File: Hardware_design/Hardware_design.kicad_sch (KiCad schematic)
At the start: 46 parts, among them IC1 ESP32-S3-WROOM-1-N16, J1 FTSH-103-01-F-D, J2 SBH11-PBPC-D05-ST-BK, J3 54-00131, SW1 TL3301FF160QG, SW2 TL3301FF160QG, U1 LS7366R-S, U2 TXB0104DR, U3 LP3875EMP-3.3

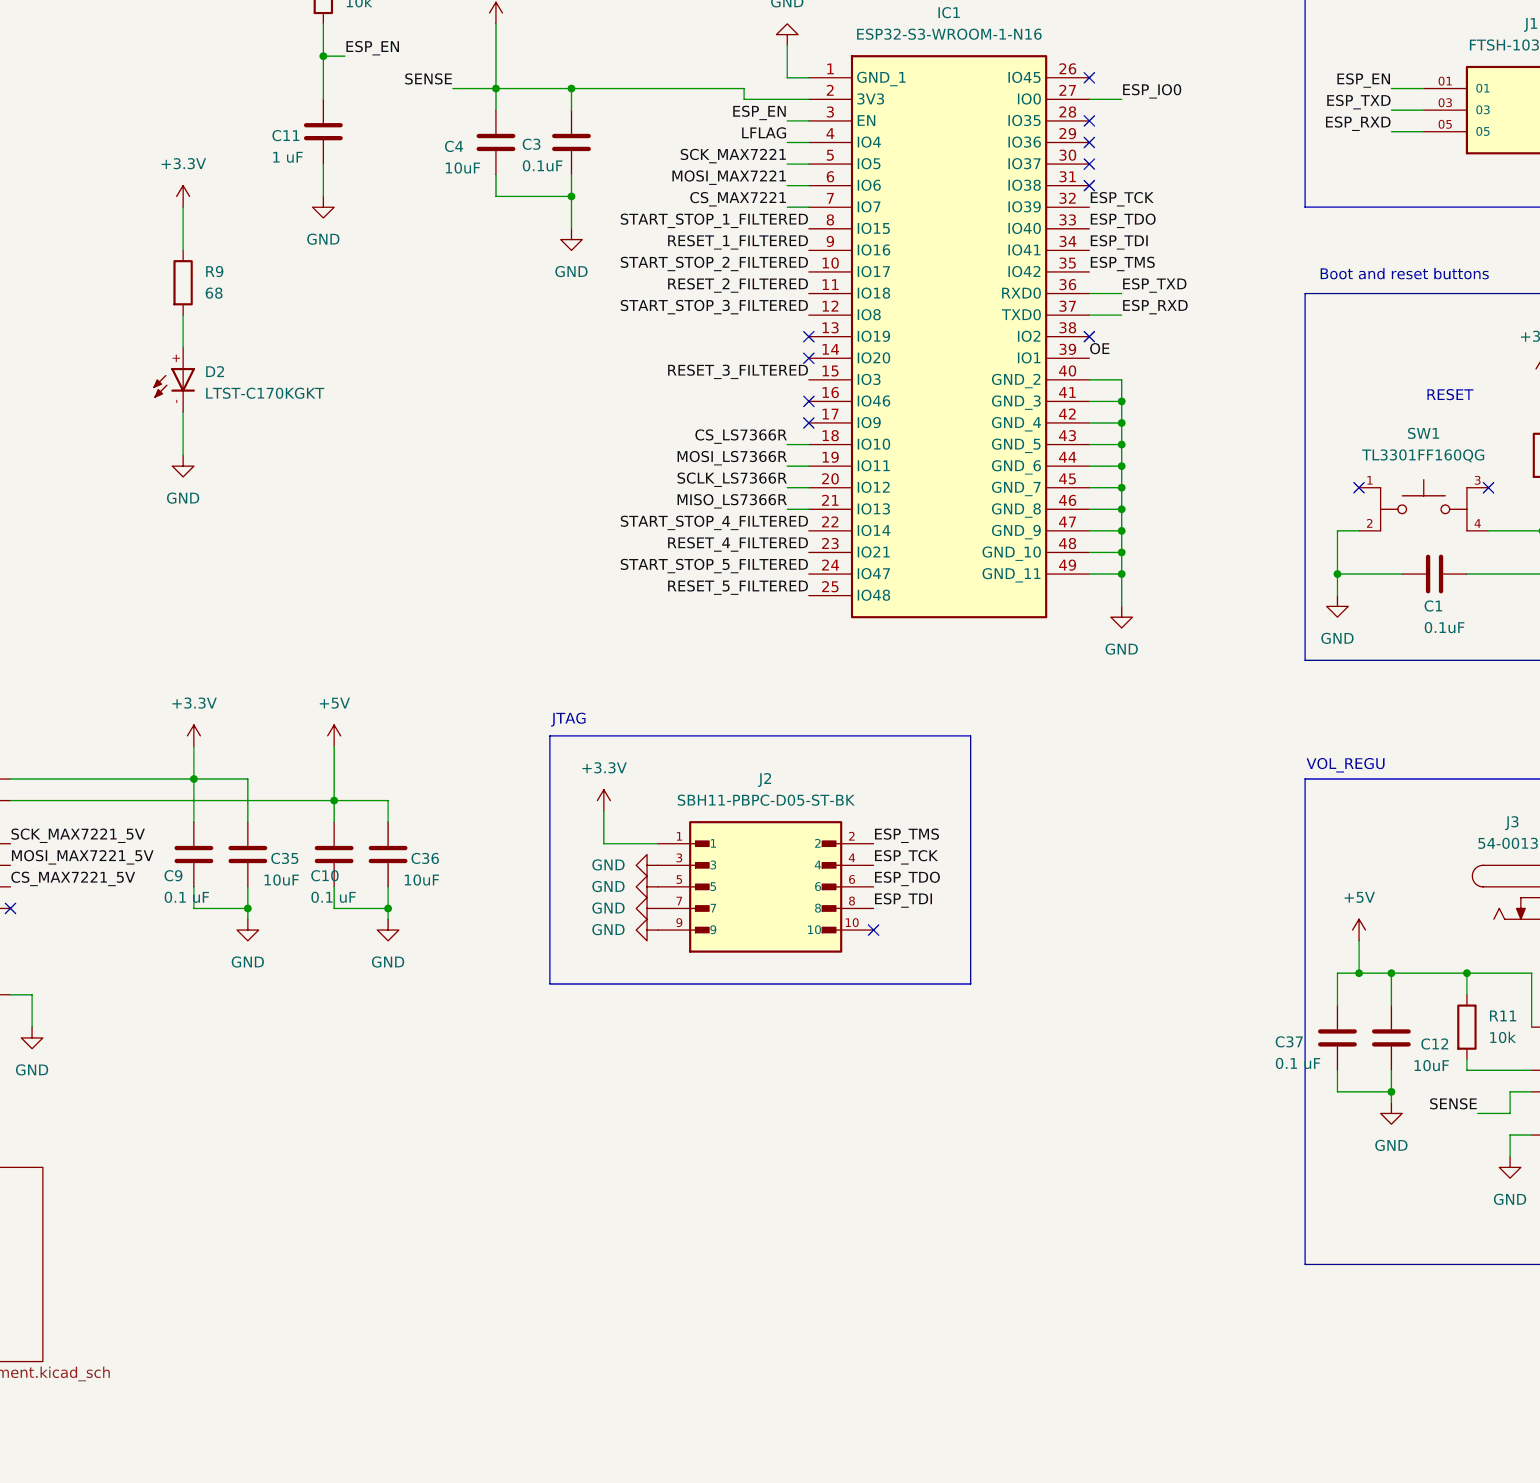
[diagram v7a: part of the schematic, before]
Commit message: component placement started
index pin and gpio pins for 10 buttons problem, index pin should be activated whenever any of the 10 buttons is pressed but only the gpio pin of the button that was pressed should also be activaded
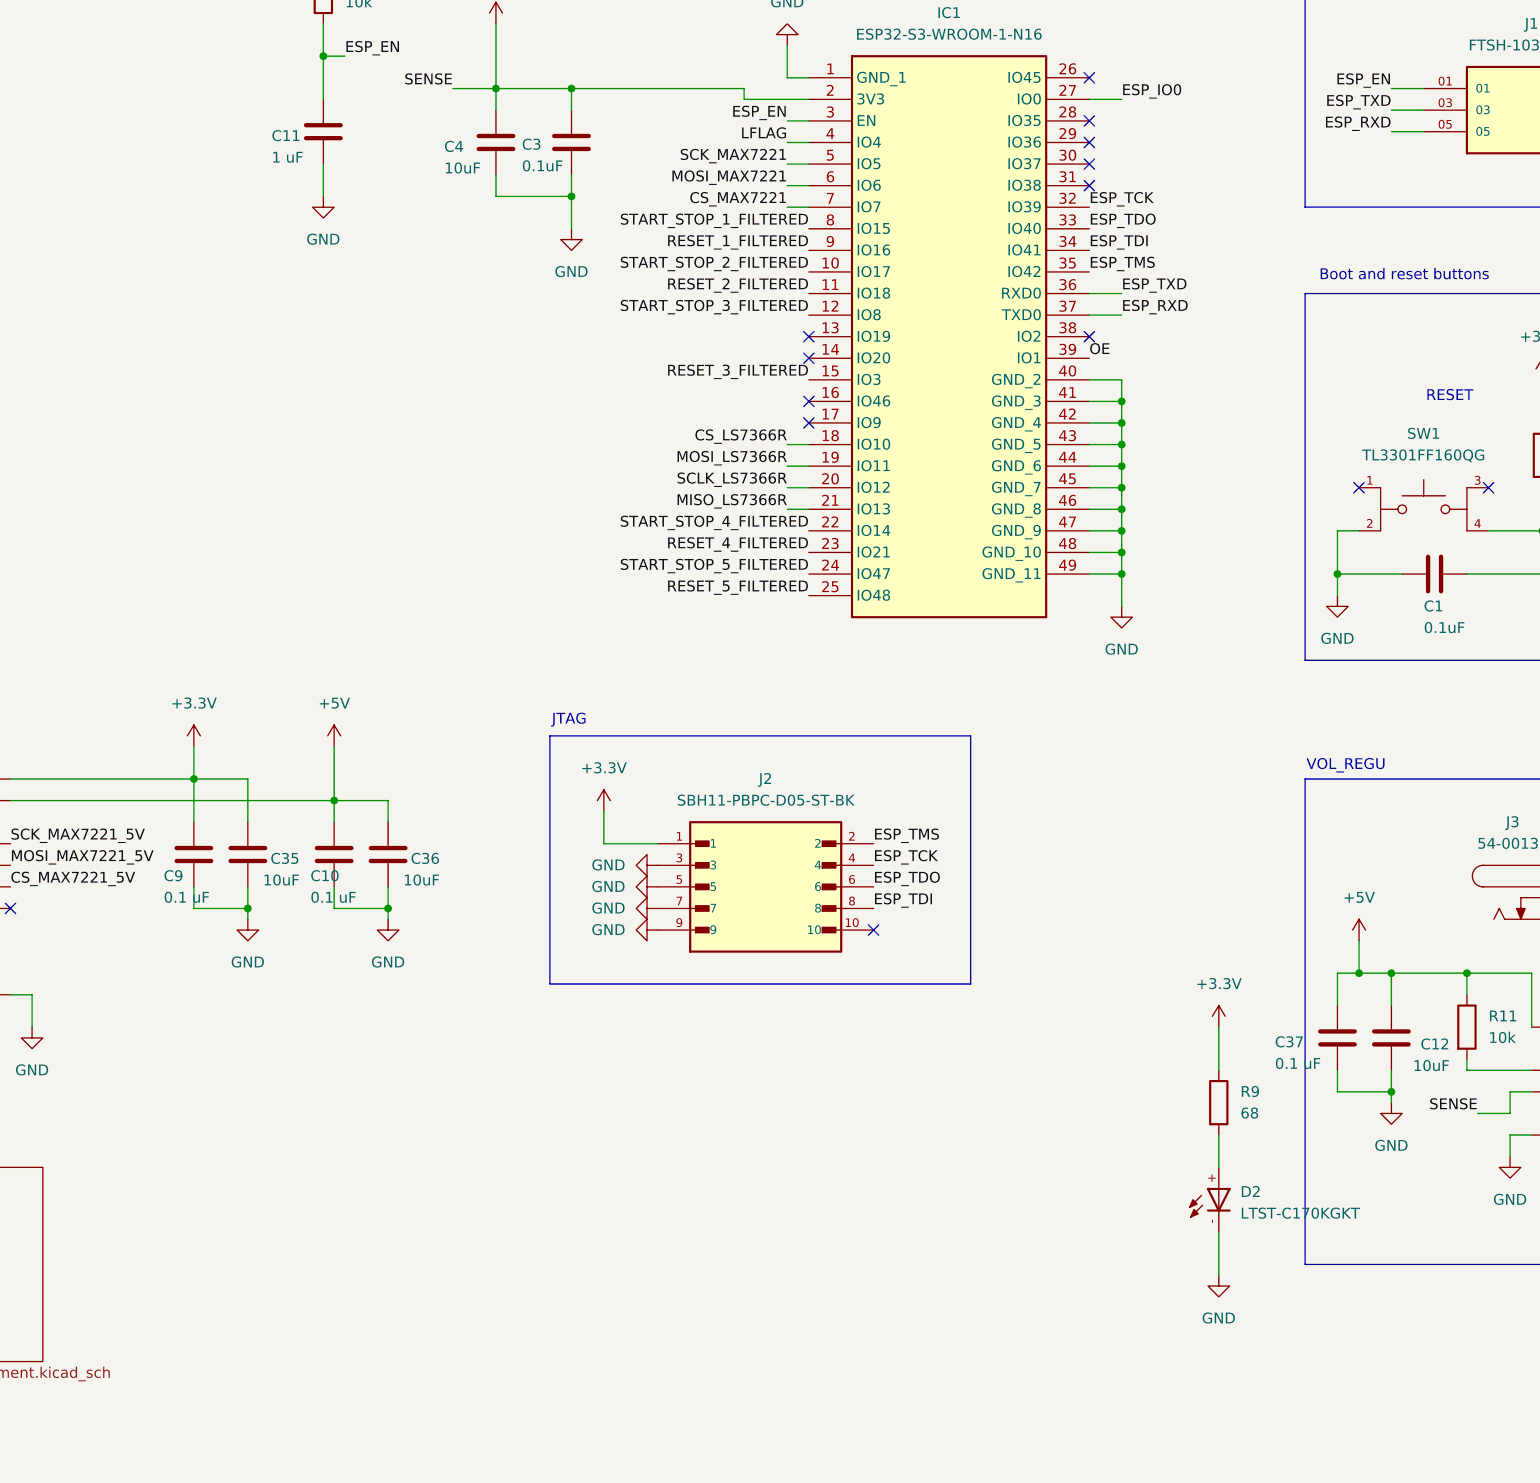
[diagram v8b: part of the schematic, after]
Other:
- moved on the sheet: D2, R9
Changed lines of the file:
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@@
 	(wire
 		(pts
-			(xy 186.69 68.58) (xy 186.69 72.39)
+			(xy 308.61 165.1) (xy 308.61 168.91)
 		)
 		(stroke
@@
 	(wire
 		(pts
-			(xy 186.69 55.88) (xy 186.69 60.96)
+			(xy 308.61 152.4) (xy 308.61 157.48)
 		)
 		(stroke
@@
 	(wire
 		(pts
-			(xy 186.69 80.01) (xy 186.69 85.09)
+			(xy 308.61 176.53) (xy 308.61 181.61)
 		)
 		(stroke
@@
 	(symbol
 		(lib_id "Device:R")
-		(at 186.69 64.77 0)
+		(at 308.61 161.29 0)
 		(unit 1)
 		(body_style 1)
@@
 		(fields_autoplaced yes)
 		(property "Reference" "R9"
-			(at 189.23 63.4999 0)
+			(at 311.15 160.0199 0)
 			(show_name no)
 			(do_not_autoplace no)
@@
 		)
 		(property "Value" "68"
-			(at 189.23 66.0399 0)
+			(at 311.15 162.5599 0)
 			(show_name no)
 			(do_not_autoplace no)
@@
 		)
 		(property "Footprint" "Footprints:0805_RES_RESC2012X60N"
-			(at 184.912 64.77 90)
+			(at 306.832 161.29 90)
 			(hide yes)
 			(show_name no)
@@
 		)
 		(property "Datasheet" ""
-			(at 186.69 64.77 0)
+			(at 308.61 161.29 0)
 			(hide yes)
 			(show_name no)
@@
 		)
 		(property "Description" "Resistor"
-			(at 186.69 64.77 0)
+			(at 308.61 161.29 0)
 			(hide yes)
 			(show_name no)
@@
 	(symbol
 		(lib_id "GREEN_LED_LTST-C170KGKT:LTST-C170KGKT")
-		(at 186.69 77.47 90)
+		(at 308.61 173.99 90)
 		(unit 1)
 		(body_style 1)
@@
 		(fields_autoplaced yes)
 		(property "Reference" "D2"
-			(at 189.23 75.2855 90)
+			(at 311.15 171.8055 90)
 			(show_name no)
 			(do_not_autoplace no)
@@
 		)
 		(property "Value" "LTST-C170KGKT"
-			(at 189.23 77.8255 90)
+			(at 311.15 174.3455 90)
 			(show_name no)
 			(do_not_autoplace no)
@@
 		)
 		(property "Footprint" "Footprints:GREEN_LED_LTST-C170KGKT"
-			(at 186.69 77.47 0)
+			(at 308.61 173.99 0)
 			(hide yes)
 			(show_name no)
@@
 		)
 		(property "Datasheet" ""
-			(at 186.69 77.47 0)
+			(at 308.61 173.99 0)
 			(hide yes)
 			(show_name no)
@@
 		)
 		(property "Description" "Green 571nm LED Indication - Discrete 2V 0805 (2012 Metric)"
-			(at 186.69 77.47 0)
+			(at 308.61 173.99 0)
 			(hide yes)
 			(show_name no)
@@
 		)
 		(property "DigiKey_Part_Number" "160-1414-1-ND"
-			(at 186.69 77.47 0)
+			(at 308.61 173.99 0)
 			(hide yes)
 			(show_name no)
@@
 		)
 		(property "SnapEDA_Link" "https://www.snapeda.com/parts/LTST-C170KGKT/Lite-On/view-part/?ref=snap"
-			(at 186.69 77.47 0)
+			(at 308.61 173.99 0)
 			(hide yes)
 			(show_name no)
@@
 		)
 		(property "Package" "0805 Lite-On"
-			(at 186.69 77.47 0)
+			(at 308.61 173.99 0)
 			(hide yes)
 			(show_name no)
@@
 		)
 		(property "Check_prices" "https://www.snapeda.com/parts/LTST-C170KGKT/Lite-On/view-part/?ref=eda"
-			(at 186.69 77.47 0)
+			(at 308.61 173.99 0)
 			(hide yes)
 			(show_name no)
@@
 		)
 		(property "MF" "Lite-On Inc."
-			(at 186.69 77.47 0)
+			(at 308.61 173.99 0)
 			(hide yes)
 			(show_name no)
@@
 		)
 		(property "MP" "LTST-C170KGKT"
-			(at 186.69 77.47 0)
+			(at 308.61 173.99 0)
 			(hide yes)
 			(show_name no)
@@
 		)
 		(property "MANUFACTURER" "LiteOn"
-			(at 186.69 77.47 0)
+			(at 308.61 173.99 0)
 			(hide yes)
 			(show_name no)
@@
 	(symbol
 		(lib_id "power:+3.3V")
-		(at 186.69 55.88 0)
+		(at 308.61 152.4 0)
 		(unit 1)
 		(body_style 1)
@@
 		(fields_autoplaced yes)
 		(property "Reference" "#PWR0123"
-			(at 186.69 59.69 0)
+			(at 308.61 156.21 0)
 			(hide yes)
 			(show_name no)
@@
 		)
 		(property "Value" "+3.3V"
-			(at 186.69 50.8 0)
+			(at 308.61 147.32 0)
 			(show_name no)
 			(do_not_autoplace no)
@@
 		)
 		(property "Footprint" ""
-			(at 186.69 55.88 0)
+			(at 308.61 152.4 0)
 			(hide yes)
 			(show_name no)
@@
 		)
 		(property "Datasheet" ""
-			(at 186.69 55.88 0)
+			(at 308.61 152.4 0)
 			(hide yes)
 			(show_name no)
@@
 		)
 		(property "Description" "Power symbol creates a global label with name \"+3.3V\""
-			(at 186.69 55.88 0)
+			(at 308.61 152.4 0)
 			(hide yes)
 			(show_name no)
@@
 	(symbol
 		(lib_id "power:GND")
-		(at 186.69 85.09 0)
+		(at 308.61 181.61 0)
 		(mirror y)
 		(unit 1)
@@
 		(fields_autoplaced yes)
 		(property "Reference" "#PWR0124"
-			(at 186.69 91.44 0)
+			(at 308.61 187.96 0)
 			(hide yes)
 			(show_name no)
@@
 		)
 		(property "Value" "GND"
-			(at 186.69 90.17 0)
+			(at 308.61 186.69 0)
 			(show_name no)
 			(do_not_autoplace no)
@@
 		)
 		(property "Footprint" ""
-			(at 186.69 85.09 0)
+			(at 308.61 181.61 0)
 			(hide yes)
 			(show_name no)
@@
 		)
 		(property "Datasheet" ""
-			(at 186.69 85.09 0)
+			(at 308.61 181.61 0)
 			(hide yes)
 			(show_name no)
@@
 		)
 		(property "Description" "Power symbol creates a global label with name \"GND\" , ground"
-			(at 186.69 85.09 0)
+			(at 308.61 181.61 0)
 			(hide yes)
 			(show_name no)
@@
 		)
 	)
-	(group ""
-		(members "1ee4661e-a290-4e5d-a427-a51335c3cdc1" "2fdad6c9-7f78-4bd3-9bf1-16232ea01b6a"
-			"30f73191-f5c0-48e7-9eee-a1949b50b4d3" "40d9613f-89cc-4831-ad89-32b0af529d14"
-			"4a275cc5-71dd-43e0-a01c-b0c5d8f7aee3" "59edbfad-7c3a-4c18-8247-28cb37d5fce3"
-			"626c8b28-06b9-41d8-84a8-2eddf9bf09f1" "6ed0385f-a35f-4639-9608-1bd68318bdec"
-			"70d52579-ef88-4488-a889-e26e689a9fc3" "79b5e6aa-2661-48aa-af87-00b07c1b856e"
-			"8c126b7e-5cba-4b6f-a829-ffec00d69f6b" "a97ffea6-128d-4874-865e-f9df81aa76ea"
-			"aa4b58b9-0870-45c7-bfce-f88d7b63c5ff" "c37b8ca4-ca8e-44d0-a58e-2fa1034771aa"
-			"d595ded7-aaf0-42d7-be14-2c0e61f9bf03" "db7f5478-3cff-4a97-9127-98828a30aaa8"
-			"fa224711-4100-45b2-8ad5-ec6b79099215" "fdf611c0-b054-4e8e-8e85-52d8c4cdfc68"
-		)
-	)
-	(group ""
-		(members "066eb391-6d68-4fb0-ac35-e859509a1dec" "1c038f46-049a-4658-9e07-0d74930b53eb"
-			"276f16a0-6a4e-4cd1-ad7a-05b2a73cc18d" "2bddc135-a2d7-4ebf-b34e-027df8d47013"
-			"2e0a79d7-2806-4e6f-b38f-a64d2e96f80e" "35e1233a-9814-40c5-a30e-1a5fab0d2788"
-			"45f09be6-001a-45f6-97c9-735c17d3d43d" "46ceb350-1017-4c06-be7c-25fb18bdb4af"
-			"48792f1b-0662-470e-8d41-7856316f976a" "4a54fef0-5572-4a8b-b823-5c17ca6b5253"
-			"53d98c9e-01f2-4557-9b8b-08164ea278ef" "55cc63df-5785-4f2b-8274-4d118ceeae29"
-			"5f437cdf-ff27-4812-8ec0-8bdbb773c9b4" "602112d8-1944-43fb-9d61-c05be01ab1eb"
-			"660b9ebf-12ff-4e61-9891-4f9841a6eaf3" "6bc34fe6-e4f5-47a1-b18d-5ffb00d0328b"
-			"7e33cc1d-cdcd-4eeb-b6d4-c91e364db6e3" "843756ad-68a1-4386-bc6b-c3a527f8bd8b"
-			"87bd9a10-d746-4ce3-a37f-0fea53975760" "88156eb7-32ff-4bf6-a8bf-34eacd647cfc"
-			"8b6690ba-f1e3-4c20-8e3c-d6a006bf73f9" "8dcdc92f-c2b3-414b-bc5c-2737c1610762"
-			"93343c8e-74d6-47ce-87d5-94dbcbbb72ce" "95215969-5d0c-4352-b8bb-9c242f03e021"
-			"988f633a-bd03-4fdb-8d83-cd7c59b30cd3" "9ba6c700-131f-4c64-864b-cb2268d02119"
-			"9bd6f628-20f2-457a-b123-58e59acba082" "a06f7ced-f020-442e-b8d1-7fa4511a9d27"
-			"a39eaa58-fe77-4c3b-84b3-913153801296" "b4677aed-6be2-4cdd-af43-0d99f0f89ec9"
-			"b4763e4c-a7e7-40db-b4e1-7542ef645937" "c12b0aca-5fbb-4596-95d4-48c9cc6d8ab5"
-			"c8e16d16-3205-4cae-baa8-2ac02a83b100" "c9ce0b80-c4dd-4c75-834c-680f6c38b769"
-			"cbbc0d2d-5a0c-464e-9daa-8f3c57663b92" "ccd12d22-ec41-4d78-9621-11700d5ccc4a"
-			"d18ae8b1-c05d-4b5d-a385-33aa4a0af76c" "e2f2801d-9305-4763-b693-898ed535ac5e"
-			"e4367474-2579-4aa1-b3c6-190d16a1813f" "e9285c43-688c-4ac3-a901-efef152565f9"
-			"f4fbe8d2-caa5-4f88-8d63-3ffcbe3b9493" "f518b59e-1ddb-4a12-8d72-fd48f23e1ca9"
-			"fba2715b-d90a-4d53-b664-567fcf38b824" "ff6bf55c-9c3d-4730-9c9d-db748508e3f2"
-		)
-	)
